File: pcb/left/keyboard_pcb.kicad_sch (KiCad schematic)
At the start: 105 parts, among them J2 Alt. Battery, J3 Alt. Switch, K00 KEYSW, K01 KEYSW, K02 KEYSW, K03 KEYSW, K04 KEYSW, K05 KEYSW, K10 KEYSW, K11 KEYSW, K12 KEYSW, K13 KEYSW, K14 KEYSW, K15 KEYSW, K20 KEYSW, K21 KEYSW, K22 KEYSW, K23 KEYSW, K24 KEYSW, K25 KEYSW, K33 KEYSW, K34 KEYSW, K35 KEYSW, U1 Flippable RP2040 ProMicro/nic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

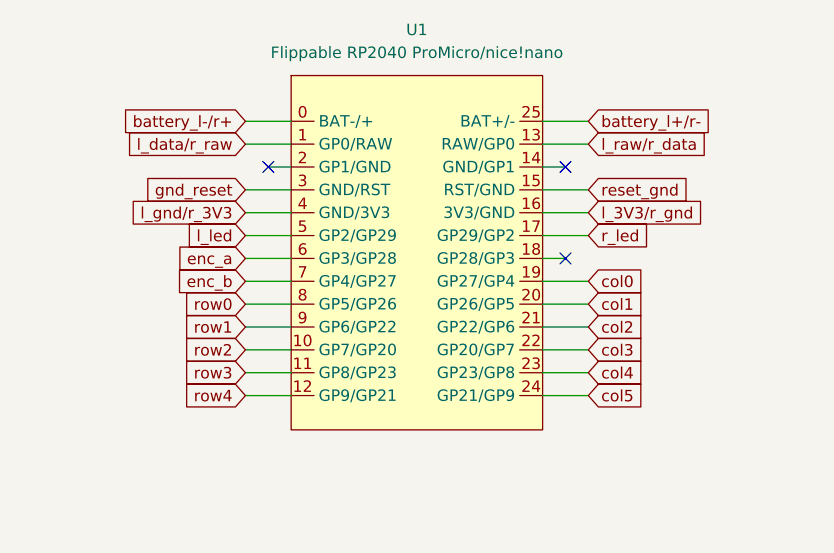
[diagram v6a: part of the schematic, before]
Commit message: Encoder B pin is now opposite Encoder A
This should mean that the pins will actually work out the same when the board is flipped.
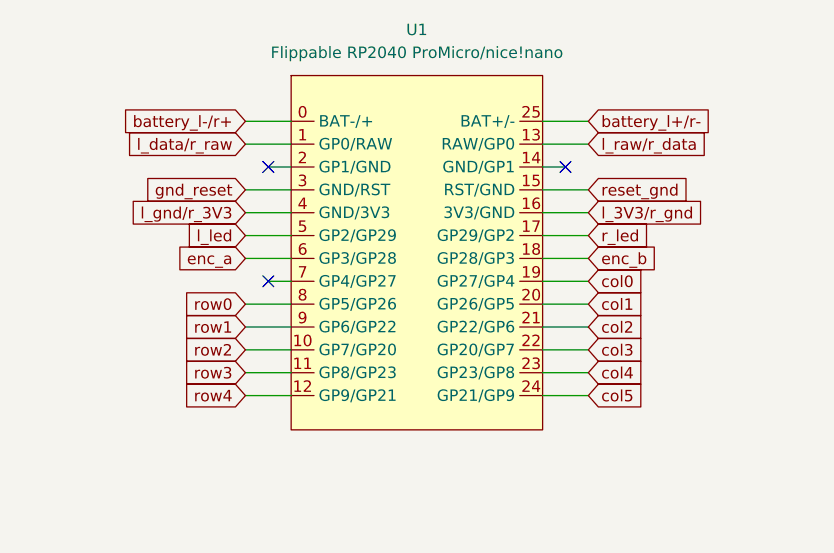
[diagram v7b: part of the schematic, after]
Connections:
- net enc_b: now also U1.18 (GP28/GP3); no longer U1.7 (GP4/GP27)
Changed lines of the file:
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@@
   )
   (no_connect (at 53.34 101.6))
-  (no_connect (at 88.9 50.8))
   (no_connect (at 55.88 40.64))
   (no_connect (at 116.84 149.86))
   (no_connect (at 53.34 129.54))
+  (no_connect (at 55.88 53.34))
   (no_connect (at 116.84 111.76))
   (no_connect (at 88.9 40.64))
@@
     (stroke (width 0) (type default))
   )
-  (wire (pts (xy 53.34 53.34) (xy 58.42 53.34))
+  (wire (pts (xy 55.88 53.34) (xy 58.42 53.34))
     (stroke (width 0) (type default))
   )
@@
     (stroke (width 0) (type default))
   )
-  (wire (pts (xy 88.9 50.8) (xy 86.36 50.8))
+  (wire (pts (xy 91.44 50.8) (xy 86.36 50.8))
     (stroke (width 0) (type default))
   )
@@
     )
   )
-  (global_label "enc_b" (shape input) (at 53.34 53.34 180) (fields_autoplaced)
-    (effects (font (size 1.27 1.27)) (justify right))
-    (property "Intersheetrefs" "${INTERSHEET_REFS}" (at 44.912 53.34 0)
-      (effects (font (size 1.27 1.27)) (justify right) hide)
-    )
-  )
   (global_label "col1" (shape input) (at 187.96 200.66 90) (fields_autoplaced)
     (effects (font (size 1.27 1.27)) (justify left))
@@
       (effects (font (size 1.27 1.27)) (justify left) hide)
     )
+  )
+  (global_label "enc_b" (shape input) (at 91.44 50.8 0) (fields_autoplaced)
+    (effects (font (size 1.27 1.27)) (justify left))
+    (property "Intersheetrefs" "${INTERSHEET_REFS}" (at 99.868 50.8 0)
+      (effects (font (size 1.27 1.27)) (justify left) hide)
+    )

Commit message: Replaced RP Pico with Pro Micro/nice!nano footprint
For space reasons, the MCU will be mounted immediately under the main PCB (with no standoffs) with the USB port facing upwards. This requires a cut-out in the PCB to allow space for the USB port and other components.
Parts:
- U1: footprint PCM_marbastlib-xp-promicroish:ProMicro_USBup -> ♥Project_Library:ProMicro_Battery_Reversible
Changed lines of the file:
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@@
       (effects (font (size 1.27 1.27)))
     )
-    (property "Footprint" "PCM_marbastlib-xp-promicroish:ProMicro_USBup" (at 71.12 80.01 0)
+    (property "Footprint" "♥Project_Library:ProMicro_Battery_Reversible" (at 71.12 80.01 0)
       (effects (font (size 1.27 1.27)) hide)
     )
